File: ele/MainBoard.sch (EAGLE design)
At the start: 122 parts, among them IC1 MCP23017SP, IC2 74HC595D, IC3 74HC595D, X1 POWER_IN, X2 POWER_OUT

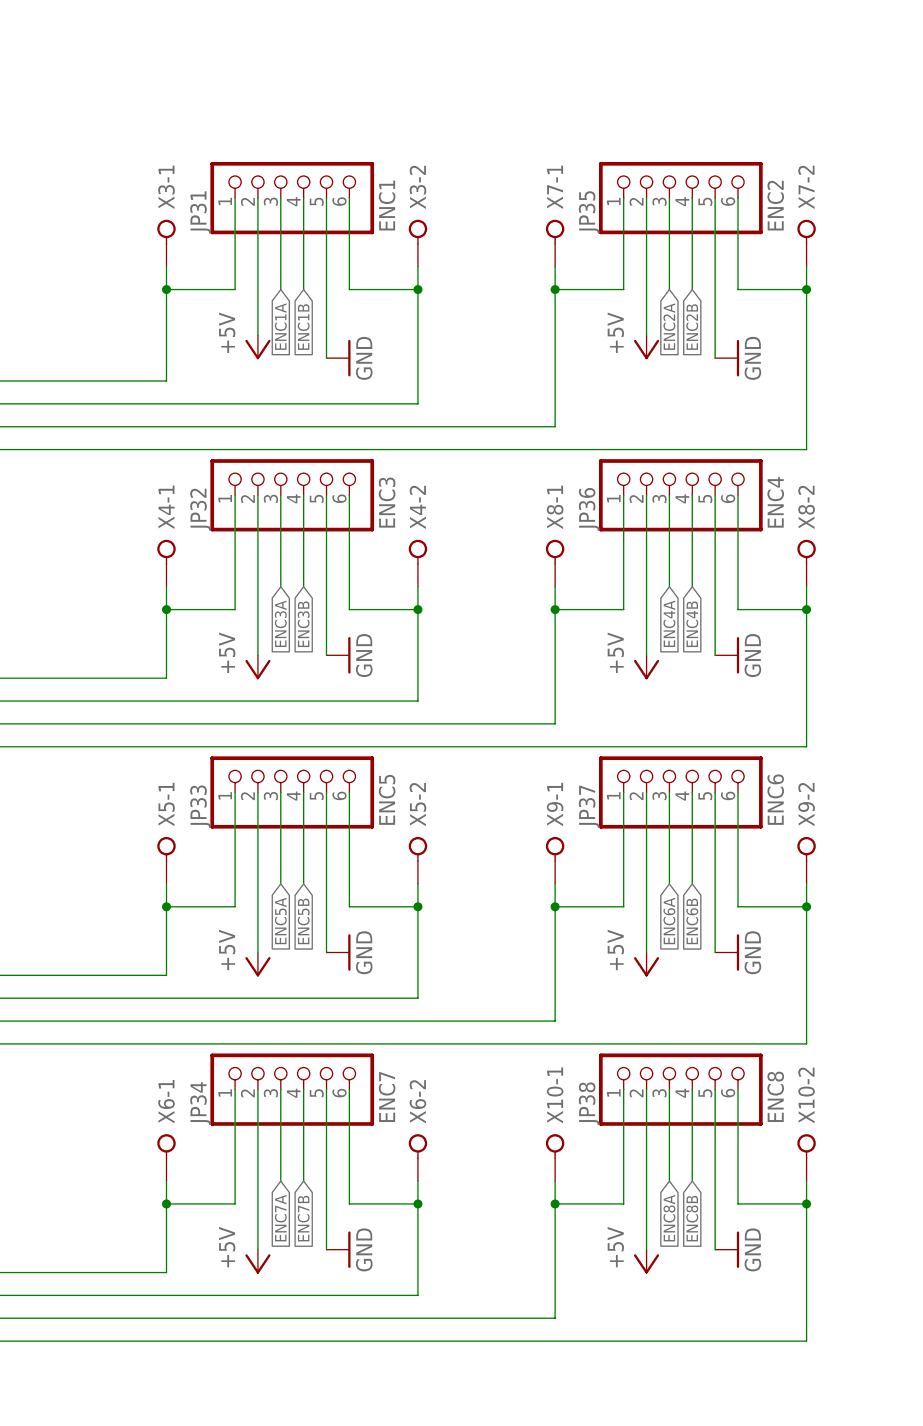
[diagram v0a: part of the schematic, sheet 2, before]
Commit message: ele: MainBoard - fix position, names, labels of motors pinheads and terminals block
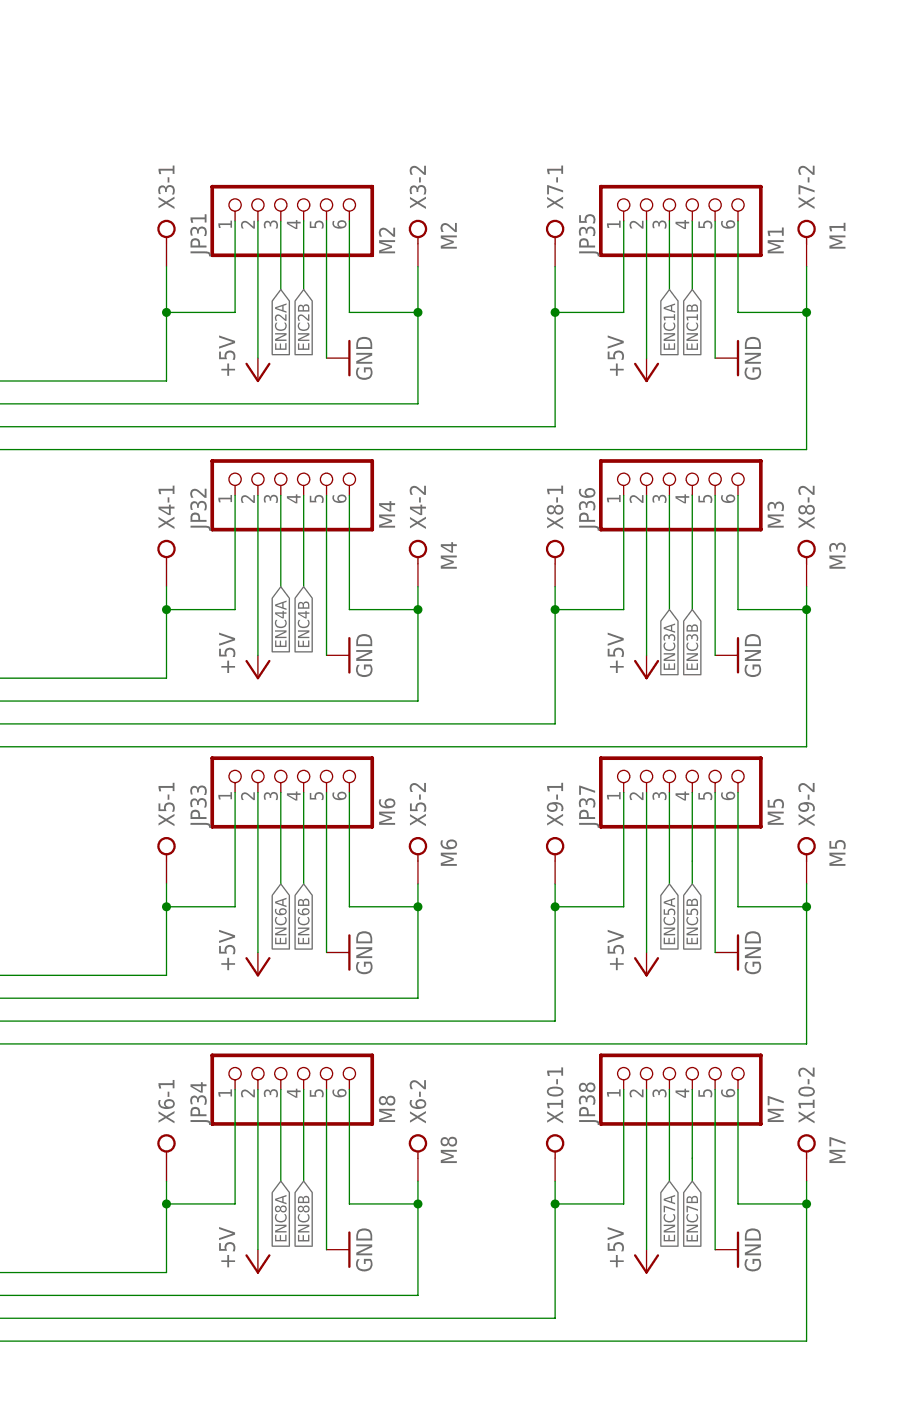
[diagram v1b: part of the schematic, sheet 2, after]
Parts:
- JP31: value ENC1 -> M2
- JP32: value ENC3 -> M4
- JP33: value ENC5 -> M6
- JP34: value ENC7 -> M8
- JP35: value ENC2 -> M1
- JP36: value ENC4 -> M3
- JP37: value ENC6 -> M5
- JP38: value ENC8 -> M7
- X10: value (none) -> M7
- X3: value (none) -> M2
- X4: value (none) -> M4
- X5: value (none) -> M6
- X6: value (none) -> M8
- X7: value (none) -> M1
- X8: value (none) -> M3
- X9: value (none) -> M5
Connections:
- net ENC1A: now also JP35.3; no longer JP31.3
- net ENC1B: now also JP35.4; no longer JP31.4
- net ENC2A: now also JP31.3; no longer JP35.3
- net ENC2B: now also JP31.4; no longer JP35.4
- net ENC3A: now also JP36.3; no longer JP32.3
- net ENC3B: now also JP36.4; no longer JP32.4
- net ENC4A: now also JP32.3; no longer JP36.3
- net ENC4B: now also JP32.4; no longer JP36.4
- net ENC5A: now also JP37.3; no longer JP33.3
- net ENC5B: now also JP37.4; no longer JP33.4
- net ENC6A: now also JP33.3; no longer JP37.3
- net ENC6B: now also JP33.4; no longer JP37.4
- net ENC7A: now also JP38.3; no longer JP34.3
- net ENC7B: now also JP38.4; no longer JP34.4
- net ENC8A: now also JP34.3; no longer JP38.3
- net ENC8B: now also JP34.4; no longer JP38.4
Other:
- moved on the sheet: JP31, JP35

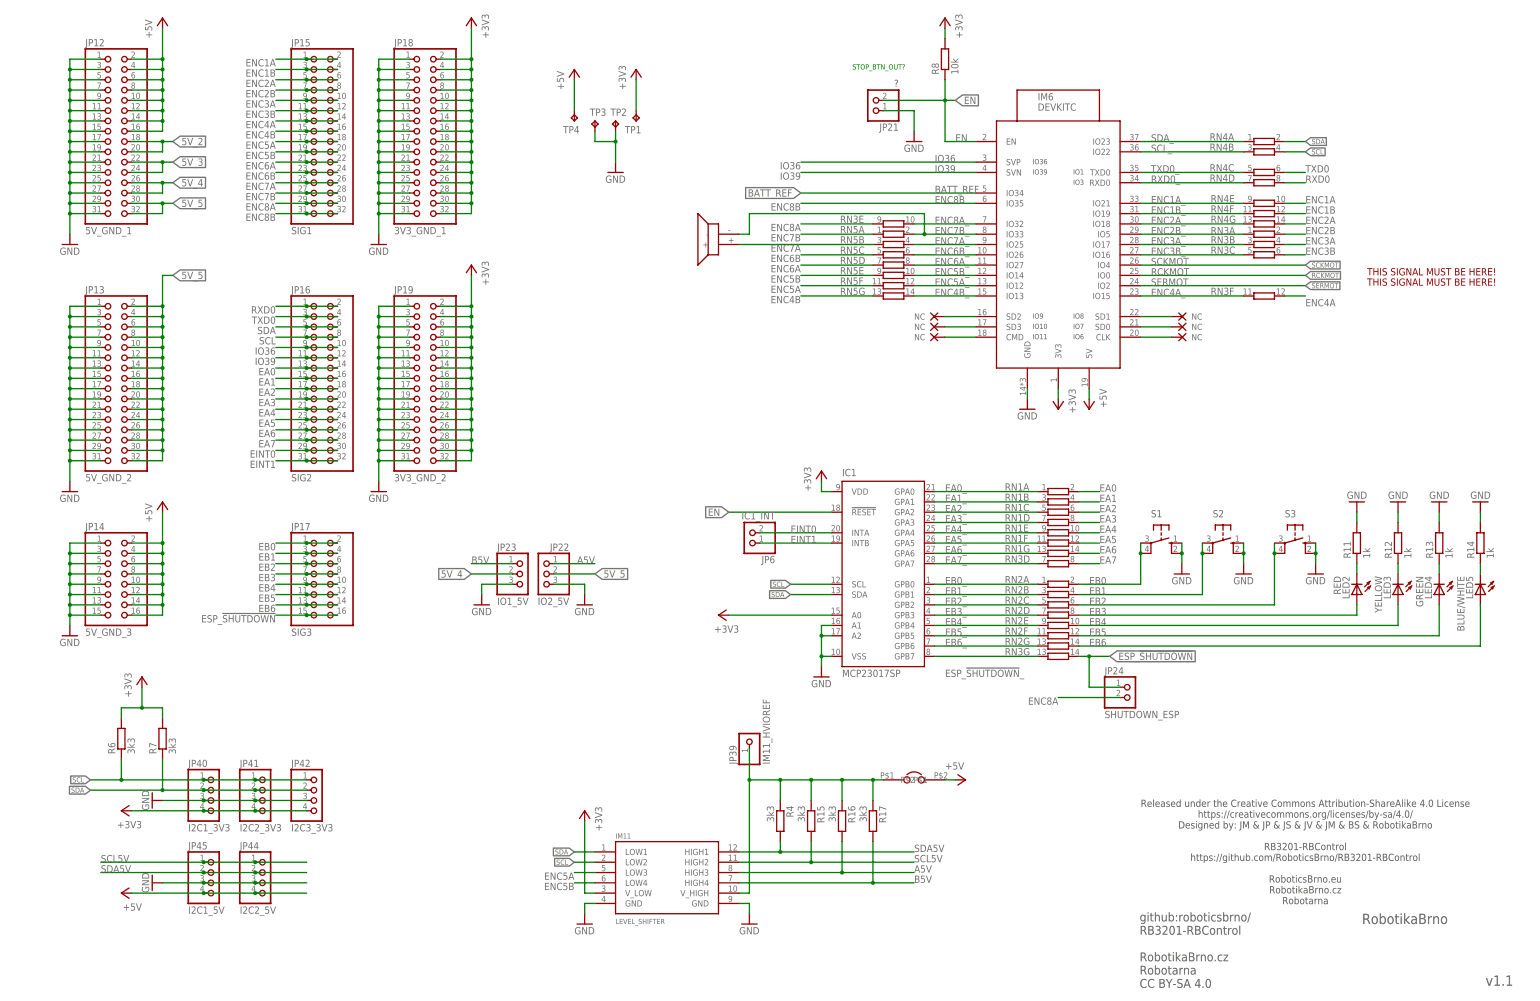
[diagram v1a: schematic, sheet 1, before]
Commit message: ele: MainBoard - add diode to ESP32 +5V, add jumper for PIEZO ON/OFF
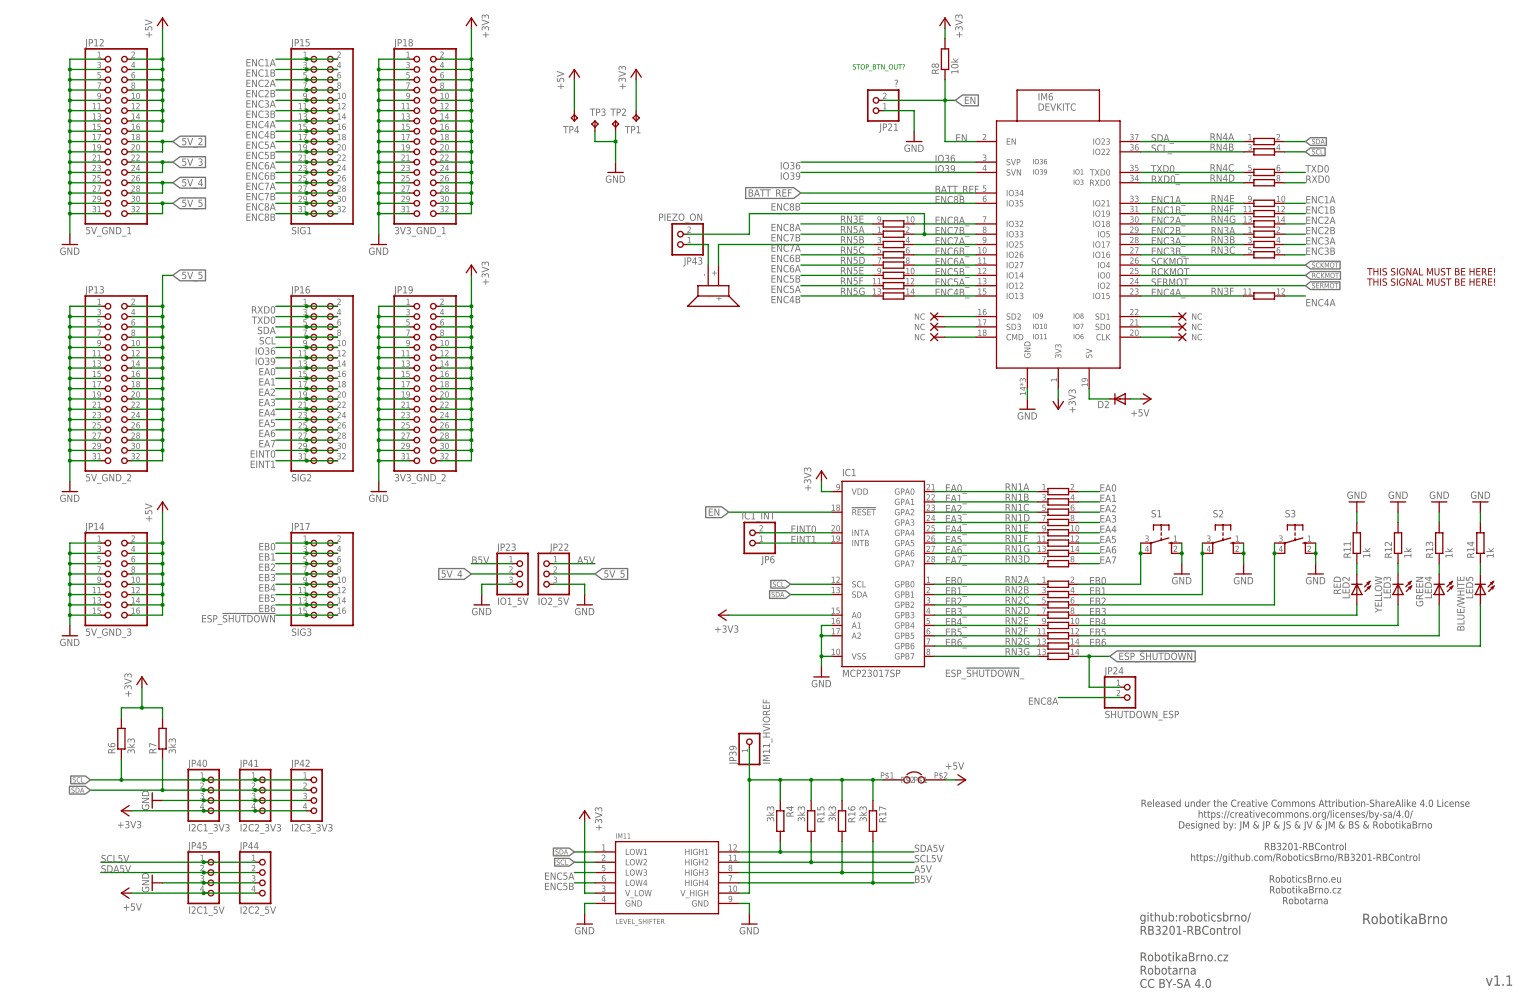
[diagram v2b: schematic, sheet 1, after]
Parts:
- added D2: (no value), diode:DIODE-SOD123
- added JP43: PIEZO_ON, pinhead:PINHD-1X2/90
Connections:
- new net +5V_ESP: D2.C, IM6.5V
- new net N$3: JP43.1, PIEZO.-
- net +5V: now also D2.A; no longer IM6.5V
- net ENC7B_: now also JP43.2; no longer PIEZO.-

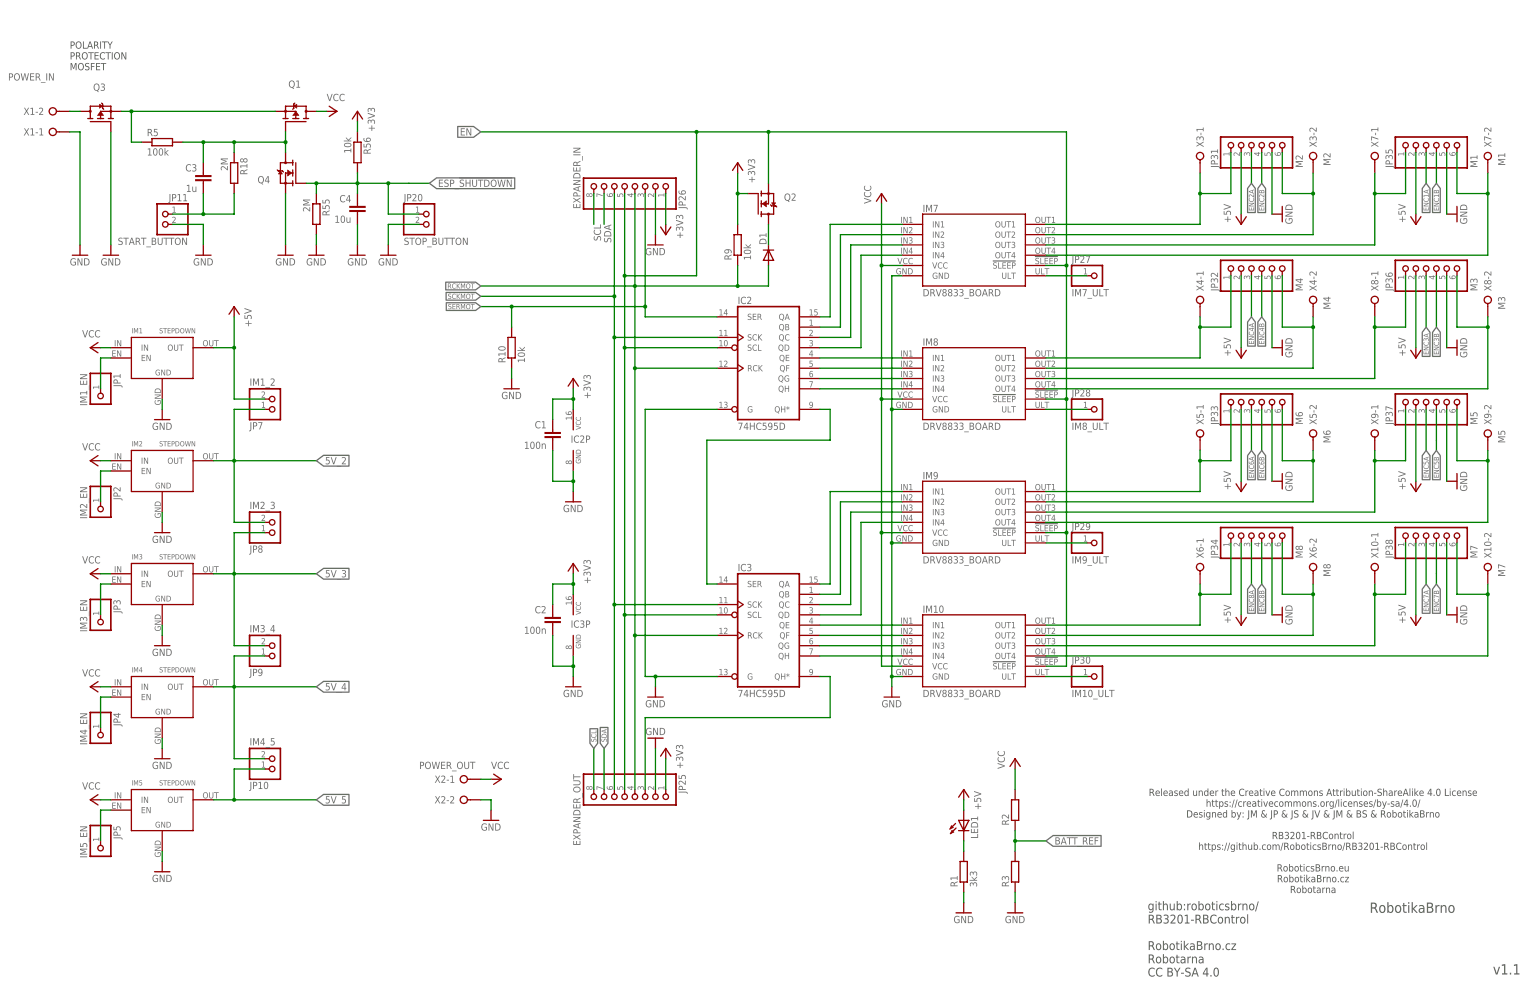
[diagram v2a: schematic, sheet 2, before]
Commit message: ele: MainBoard - repair problem with pin IO12, change nets around piezo, change some names and labels
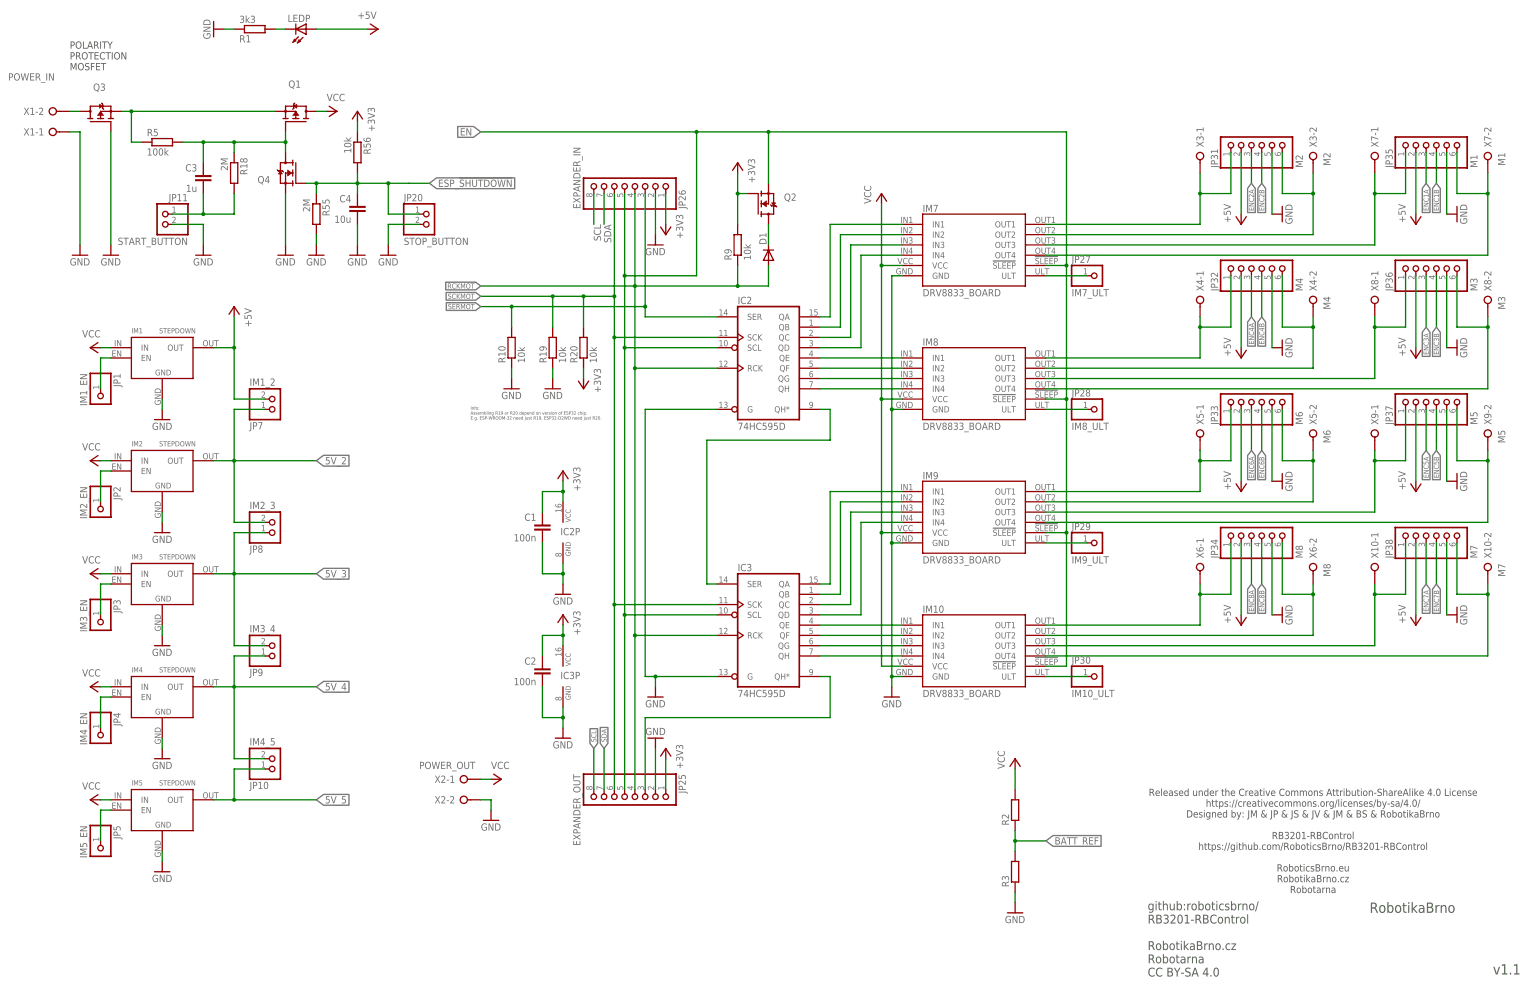
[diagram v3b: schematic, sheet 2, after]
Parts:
- removed LED5: BLUE/WHITE, led:LED3MM
- added LEDP: (no value), led:LED3MM
- added R19, R20: 10k, rcl_upravena:R-EU_0204/2V
- JP21: value ? -> RESET
- LED1: value (none) -> RED
- LED2: value RED -> YELLOW
- LED3: value YELLOW -> GREEN
- LED4: value GREEN -> BLUE/WHITE
- renumbered S1 to SW1, S2 to SW2, S3 to SW3
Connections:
- net N$3 renamed PIEZO
- removed net N$10: LED2.C, R11.1
- removed net N$15: LED3.C, R12.1
- removed net N$16: LED4.C, R13.1
- removed net N$17: LED5.C, R14.1
- new net LED1: LED1.C, R11.1
- new net LED2: LED2.C, R12.1
- new net LED3: LED3.C, R13.1
- new net LED4: LED4.C, R14.1
- net +3V3: now also R20.1
- net +5V: now also LEDP.A; no longer LED1.A
- net EB3: now also LED1.A; no longer LED2.A
- net EB4: now also LED2.A; no longer LED3.A
- net EB5: now also LED3.A; no longer LED4.A
- net EB6: now also LED4.A; no longer LED5.A
- net ENC5A: now also RN5F.2; no longer RN5F.1
- net ENC5A_: now also IM6.IO4, RN5F.1; no longer IM6.IO12, RN5F.2
- net ENC7A: now also JP43.2; no longer PIEZO.+
- net ENC7B_: now also PIEZO.+; no longer JP43.2
- net GND: now also R19.1
- net N$9: now also LEDP.C; no longer LED1.C
- net SCKMOT: now also IM6.IO12, R19.2, R20.2; no longer IM6.IO4
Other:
- note added: "Info: Assembling R19 or R20 depend on version of ESP32 chip. E.g. ESP-WROOM-32 need just R19, ESP32-D2WD need just R20."
- note removed: "STOP_BTN_OUT?"
- moved on the sheet: C1, C2, IC2P, IC3P, JP43, LED2, LED3, LED4, R1, RN5F
